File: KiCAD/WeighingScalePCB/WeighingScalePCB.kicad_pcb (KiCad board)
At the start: 2 copper layers, 94.6 x 73.3 mm, 64 parts, among them IC1 MAX6675ISA+T, IC2 APS11753KMDALX-9PL5, J1 Conn_01x14_MountingPin, J2 AudioJack4, J4 Battery Conn, J6 Conn_01x04_MountingPin, Q2 NX138AKR, Q3 NX138AKR, Q4 NX138AKR, Q5 NX138AKR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

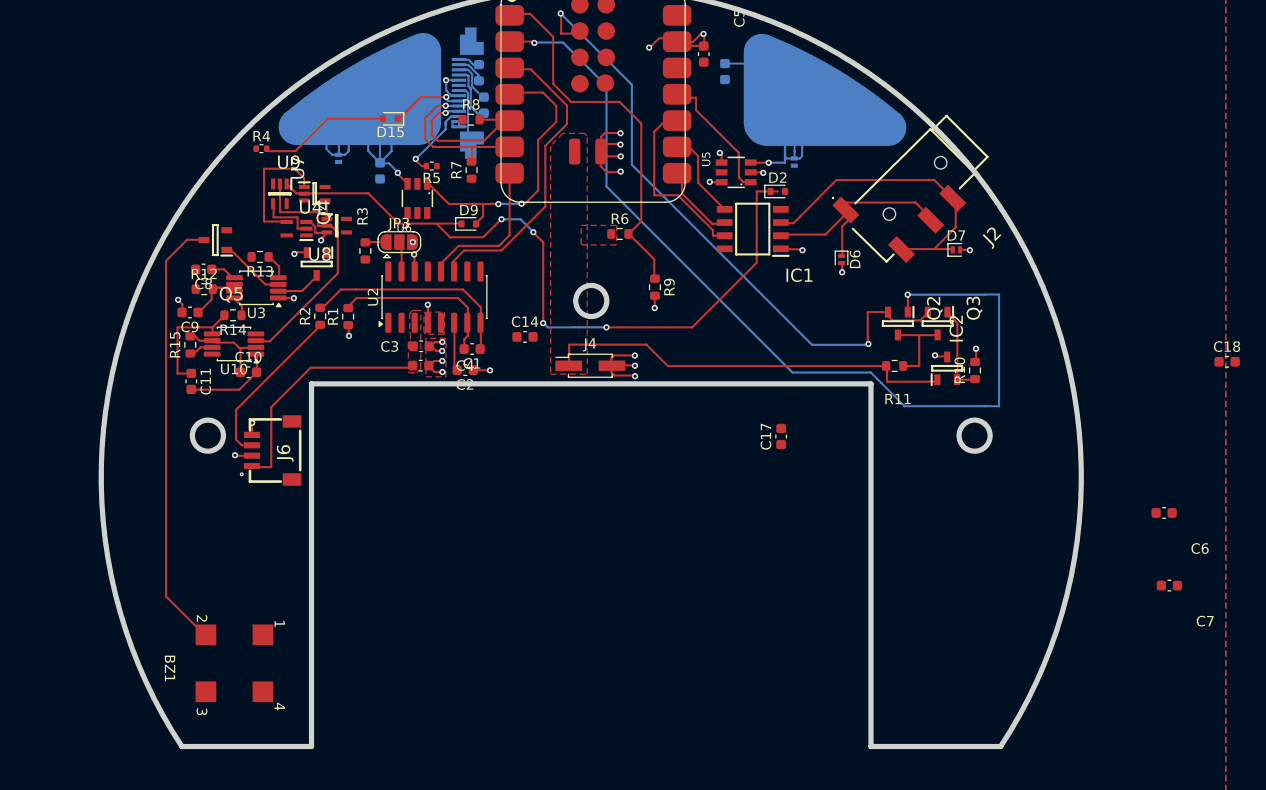
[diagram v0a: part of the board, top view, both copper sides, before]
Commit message: cleared all islands and unconnected GNDs, drc and erc pending, ferrite pending, linked 3d for thermocouple amp, touchpad ic and xiao
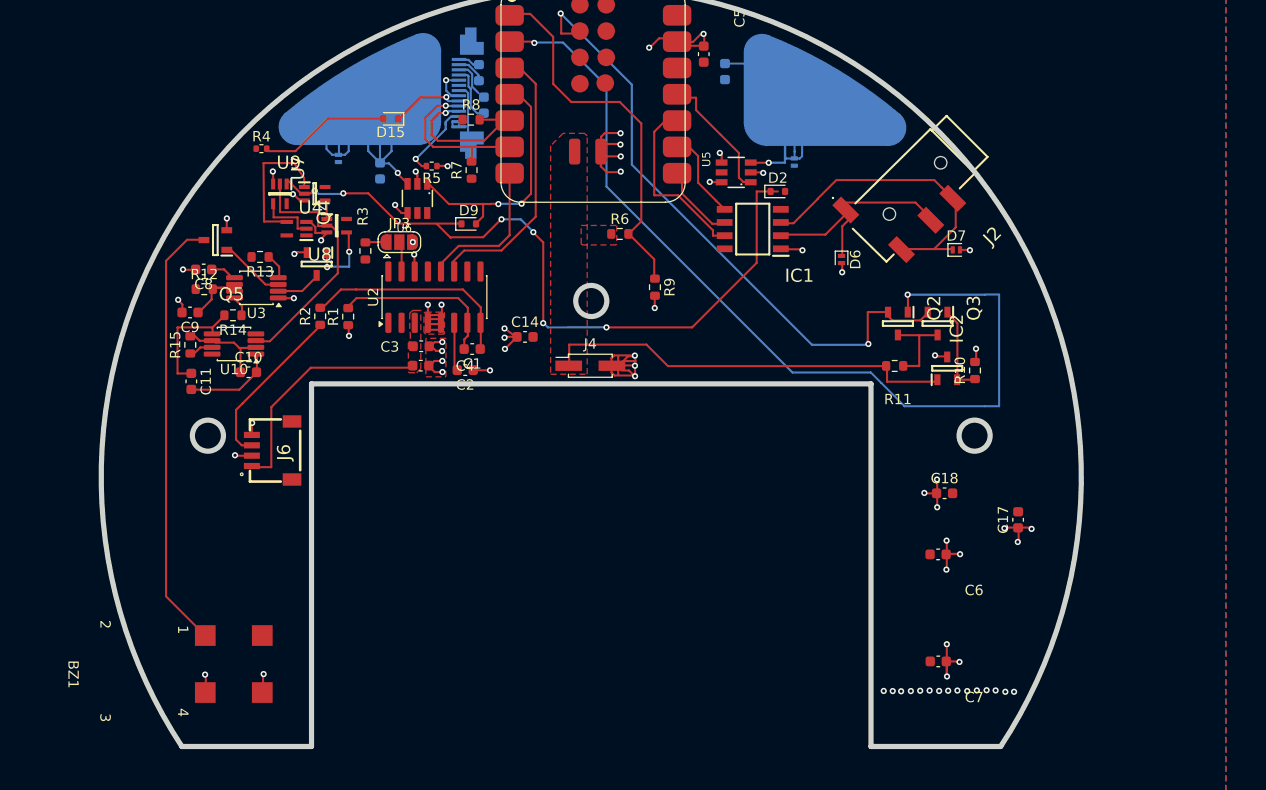
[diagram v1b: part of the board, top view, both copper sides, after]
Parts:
- moved C18 30.1 mm to (181.0, 85.6)
- moved C17 24.2 mm to (188.1, 88.2)
- moved C7 23.5 mm to (180.4, 101.9)
- moved C6 22.2 mm to (180.4, 91.5)
- moved BZ1 9.33 mm to (103.1, 102.6)
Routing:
- net GND: vias 33 -> 73
- net /timeORtare: vias 4 -> 6
- net /buzzer trigger: vias 0 -> 2

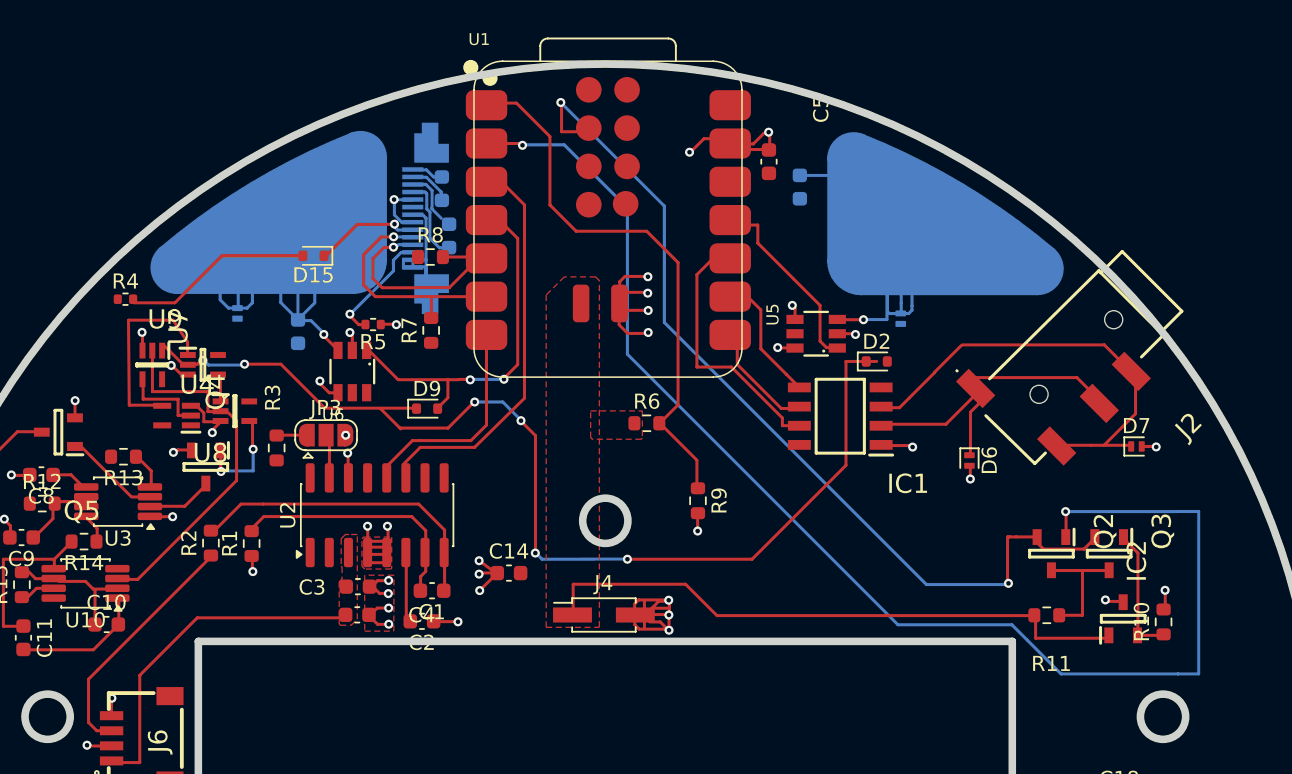
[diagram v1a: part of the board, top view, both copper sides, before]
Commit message: fb removed, decaps will be sufficient, add more decaps, add cap between vbat and vcc
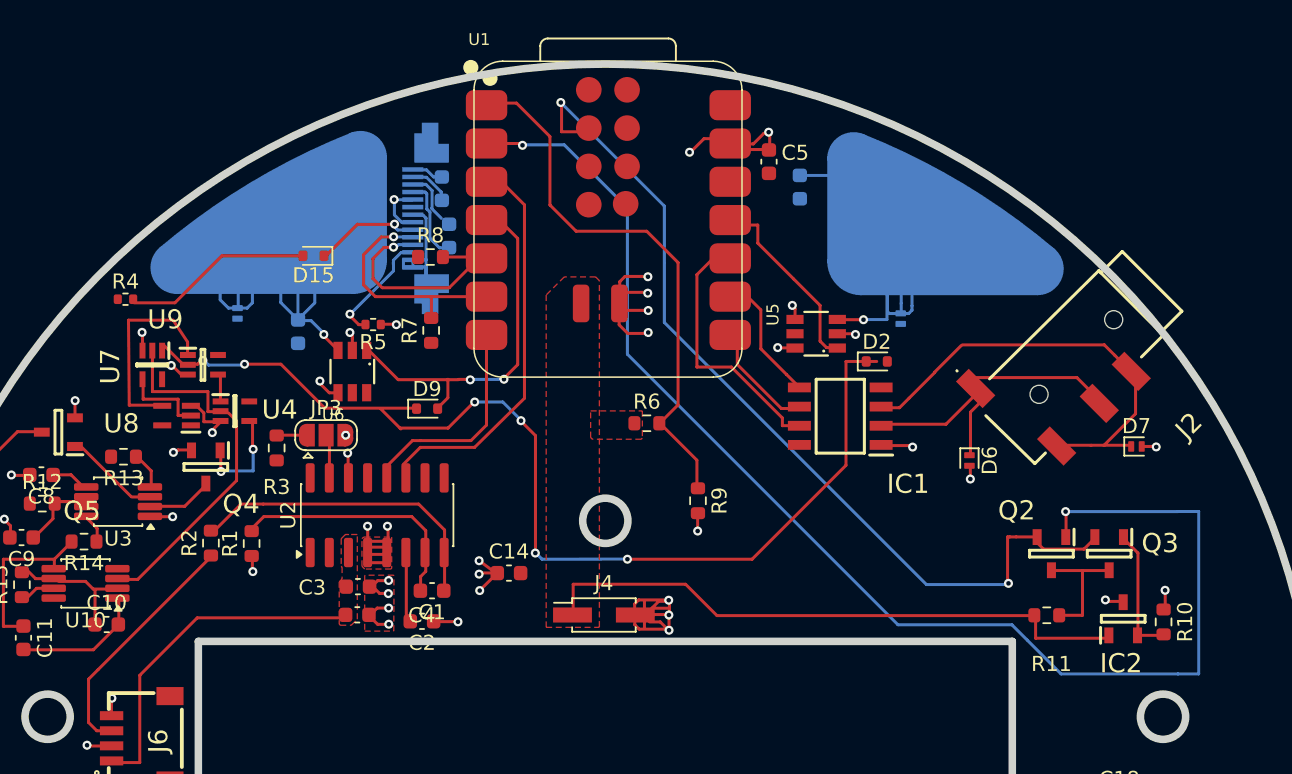
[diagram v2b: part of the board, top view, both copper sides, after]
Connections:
- C3 pad 2: /DVDD_ldcell -> VCC
- C4 pad 2: /DVDD_ldcell -> VCC
- J6 pad 1: /DVDD_ldcell -> VCC
- U2 pad 3: /DVDD_ldcell -> VCC
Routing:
- removed copper zone on F.Cu, net /DVDD_ldcell

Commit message: dxf to be updated, start design verification document next
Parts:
- moved C7 81.3 mm to (112.8, 56.7), turned to 90 degrees
- moved C6 78.7 mm to (103.5, 74.8), turned to 90 degrees
- moved C17 28.9 mm to (168.8, 66.6), turned to -90 degrees
- moved BZ1 20.9 mm to (96.8, 82.7)
- moved C18 14.1 mm to (189.9, 74.6), turned to 90 degrees
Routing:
- net GND: vias 73 -> 56

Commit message: all 3d added
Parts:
- moved C13 6.45 mm to (143.0, 48.6)
- moved C12 6.17 mm to (142.2, 44.5)
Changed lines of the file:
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@@
 		)
 		(group ""
-			(members "506a4490-bf3e-4c77-b169-08c29425c1eb" "5a118c7e-b5fb-4519-b66b-15accd4b80eb"
-				"6aae3fa3-525f-4afb-8aeb-590de53548be" "cf3bb025-e151-42ab-9bc5-0ee6cbb9af20"
-				"ebccb0a9-73e8-42e9-8617-28dd7e6247ca" "f4d772ca-2c29-4b5a-9d41-ad5a91ca73c4"
+			(members "068117ea-2ab3-4103-ba16-efab7a55a031" "22f2eacf-efce-438e-8243-23edad42cc39"
+				"6f3542f6-99f9-4a27-9b4c-fb9414b0d3b7" "7efa6883-bdff-4493-9e70-ba8cbb57e1ac"
+				"97dd7b8d-34f9-4bca-9663-b7264ed983fc" "d30c1f34-a56e-4f72-b701-78a4600fa9d7"
 			)
 		)
 		(group ""
-			(members "04d87761-6831-450b-a97a-65f3a226a256" "1311b18f-d4b6-42da-a0fc-41010944ea85"
-				"462201b0-c7be-4960-8844-6b6941b4ad2f" "6b9a12f5-451e-4911-b646-67a0598808ab"
-				"795389ad-acfc-4cde-b23d-8961354a9e65" "f49f4621-66a9-4145-a56a-5194f2d1576a"
+			(members "6514d6e0-6418-42fa-a38c-0725f87867d9" "6de8367c-d1df-4f82-a835-7e814d5bfa49"
+				"8147b97e-7544-4fa4-8697-c19391ba267f" "8179ba7d-6855-406b-b541-e840262d3c66"
+				"bbcafd73-0455-4559-b592-1946e72bc132" "db8d633d-4ceb-4d6e-b012-186990593e7a"
 			)
 		)
@@
 			)
 		)
+		(model "/home/chinmay/Projects/weighing_scale/Weighing-Scale-Coaster/KiCAD/WeighingScaleLibrary/LIB_SN74LVC1G04DCKR/SN74LVC1G04DCKR/3D/SN74LVC1G04DCKR.stp"
+			(offset
+				(xyz 0 0 0)
+			)
+			(scale
+				(xyz 1 1 1)
+			)
+			(rotate
+				(xyz 0 0 0)
+			)
+		)
 	)
 	(footprint "Footprints:SOT95P230X110-3N"
@@
 		)
 		(group ""
-			(members "04db45b0-54de-4ecb-b3c5-1046cf09671d" "441535aa-b818-4581-b5c3-c87ac78df74a"
-				"70dec69a-c15a-464d-b816-58cd609b9641" "a5ce6d7f-2c60-41db-8497-8040c0a304c2"
-				"e7423acd-4a56-4767-94b4-65c8eac0399b" "f55c3de0-39ea-4c4e-b807-f996b29d4372"
+			(members "56c2c2f2-41dc-4893-9ead-193c833977ec" "6f2889ef-8d5d-40c0-b0f0-e2c4b89dda04"
+				"70a92687-e41e-4280-9e15-a43491f83443" "79975846-58ba-4aca-bff2-32609abe09fe"
+				"9baa09ee-731b-4587-abcf-bb5f4ec44fb7" "ba98ae2b-0f4b-4403-9b40-e543a76478a0"
 			)
 		)
 		(group ""
-			(members "68e8b008-a0a5-43cd-b1f3-88e8a99a1445" "6ee33438-7f2b-4413-aa9f-a5a94c786fa7"
-				"7da6b385-5ffd-42e1-88ea-2362b0d28c88" "ac952bc0-21e2-4a34-98fa-b647f0e50b6c"
-				"b40dbc47-c785-419d-96d3-5da5963c95b4" "b410ba7d-2c2c-4c5e-af11-e89df746a8c0"
+			(members "2081a35a-ca3f-4472-a093-8e58f7bb1505" "445a45a7-f8a9-4c7b-834b-4eeea78861cd"
+				"66a930b3-a878-4489-8dda-2250efdb7383" "bb93f1d3-c7dd-4468-ba06-857c31f5a8c2"
+				"c3e7985c-49ec-4598-9838-d6b2f6419484" "f8dbbecf-a25a-4567-ba35-142d3adba851"
 			)
 		)
@@
 			)
 		)
+		(model "/home/chinmay/Projects/weighing_scale/Weighing-Scale-Coaster/KiCAD/WeighingScaleLibrary/LIB_74LVC1G79GW,125/74LVC1G79GW,125/3D/74LVC1G79GW,125.stp"
+			(offset
+				(xyz 1.5 0.9 -0.8)
+			)
+			(scale
+				(xyz 1 1 1)
+			)
+			(rotate
+				(xyz -90 -0 90)
+			)
+		)
 	)
 	(footprint "Diode_SMD:D_SOD-523"
@@
 			)
 		)
+		(model "/home/chinmay/Projects/weighing_scale/Weighing-Scale-Coaster/KiCAD/WeighingScaleLibrary/LIB_JST_SM04B-SRSS-TB_LF__SN_/SM04B-SRSS-TB_LF__SN_/3D/SM04B-SRSS-TB_LF__SN_.stp"
+			(offset
+				(xyz 3 4 -0.5)
+			)
+			(scale
+				(xyz 1 1 1)
+			)
+			(rotate
+				(xyz -90 -0 -0)
+			)
+		)
 	)
 	(footprint "Footprints:SOT95P240X115-3N_Hall effect"
@@
 			)
 		)
+		(model "/home/chinmay/Projects/weighing_scale/Weighing-Scale-Coaster/KiCAD/WeighingScaleLibrary/LIB_74LVC1G79GW,125/74LVC1G79GW,125/3D/74LVC1G79GW,125.stp"
+			(offset
+				(xyz 1.5 0.9 -0.8)
+			)
+			(scale
+				(xyz 1 1 1)
+			)
+			(rotate
+				(xyz -90 -0 90)
+			)
+		)
 	)
 	(footprint "Resistor_SMD:R_0603_1608Metric"
@@
 			)
 		)
+		(model "/home/chinmay/Projects/weighing_scale/Weighing-Scale-Coaster/KiCAD/WeighingScaleLibrary/LIB_SFV14R-3STBE1HLF/SFV14R-3STBE1HLF/3D/SFV14R-3STBE1HLF.stp"
+			(offset
+				(xyz 5.45 -4.3 2)
+			)
+			(scale
+				(xyz 1 1 1)
+			)
+			(rotate
+				(xyz 90 -0 180)
+			)
+		)
 	)
 	(footprint "Capacitor_SMD:C_0603_1608Metric"
 		(layer "B.Cu")
-		(at 136.04 45.035 90)
+		(at 142.19 44.48 90)
 		(descr "Capacitor SMD 0603 (1608 Metric), square (rectangular) end terminal, IPC-7351 nominal, (Body size source: IPC-SM-782 page 76, https://www.pcb-3d.com/wordpress/wp-content/uploads/ipc-sm-782a_amendment_1_and_2.pdf), generated with kicad-footprint-generator")
 		(tags "capacitor")
@@
 	(footprint "Capacitor_SMD:C_0603_1608Metric"
 		(layer "B.Cu")
-		(at 136.52 48.17 -90)
+		(at 142.96 48.58 -90)
 		(descr "Capacitor SMD 0603 (1608 Metric), square (rectangular) end terminal, IPC-7351 nominal, (Body size source: IPC-SM-782 page 76, https://www.pcb-3d.com/wordpress/wp-content/uploads/ipc-sm-782a_amendment_1_and_2.pdf), generated with kicad-footprint-generator")
 		(tags "capacitor")
@@
 	)
 	(gr_line
+		(start 141.44 43.77)
+		(end 142.21 43.77)
+		(stroke
+			(width 0.2)
+			(type default)
+		)
+		(layer "B.Cu")
+		(net 39)
+	)
+	(gr_line
 		(start 164.02 53.72)
 		(end 165.57 53.72)
@@
 	)
 	(gr_line
+		(start 136.62 48.96)
+		(end 141.52 48.96)
+		(stroke
+			(width 0.2)
+			(type default)
+		)
+		(layer "B.Cu")
+		(net 61)
+	)
+	(gr_line
 		(start 167.23 53.1)
 		(end 167.23 52.8)
@@
 	)
 	(gr_line
+		(start 140.95 44.26)
+		(end 141.44 43.77)
+		(stroke
+			(width 0.2)
+			(type default)
+		)
+		(layer "B.Cu")
+		(net 39)
+	)
+	(gr_line
+		(start 135.64 46.6)
+		(end 135.64 47.69)
+		(stroke
+			(width 0.2)
+			(type default)
+		)
+		(layer "B.Cu")
+		(net 60)
+	)
+	(gr_line
 		(start 134.99 50.23)
 		(end 134.99 51.13)
@@
 	)
 	(gr_line
+		(start 135.39 46.35)
+		(end 135.64 46.6)
+		(stroke
+			(width 0.2)
+			(type default)
+		)
+		(layer "B.Cu")
+		(net 60)
+	)
+	(gr_line
 		(start 127.61 52.61)
 		(end 127.61 51.65)
@@
 	)
 	(gr_line
+		(start 141.52 48.96)
+		(end 142.03 49.47)
+		(stroke
+			(width 0.2)
+			(type default)
+		)
+		(layer "B.Cu")
+		(net 61)
+	)
+	(gr_line
 		(start 134.16 44.75)
 		(end 134.98 44.75)
@@
 	)
 	(gr_line
+		(start 136 45.26)
+		(end 142.21 45.26)
+		(stroke
+			(width 0.2)
+			(type default)
+		)
+		(layer "B.Cu")
+		(net 38)
+	)
+	(gr_line
 		(start 134.99 51.13)
 		(end 134.99 49.75)
@@
 	)
 	(gr_line
+		(start 142.03 49.47)
+		(end 142.96 49.47)
+		(stroke
+			(width 0.2)
+			(type default)
+		)
+		(layer "B.Cu")
+	)
+	(gr_line
 		(start 134.15 49.27)
 		(end 133.34 49.27)
@@
 		)
 		(layer "B.Cu")
+		(net 61)
 	)
 	(gr_line
@@
 	)
 	(gr_line
+		(start 135.64 47.69)
+		(end 142.94 47.69)
+		(stroke
+			(width 0.2)
+			(type default)
+		)
+		(layer "B.Cu")
+	)
+	(gr_line
 		(start 123.12 52.96)
 		(end 123.47 52.61)
@@
 	)
 	(gr_line
-		(start 134.1 44.28)
-		(end 135.02 44.28)
+		(start 136.08 44.26)
+		(end 140.95 44.26)
 		(stroke
 			(width 0.2)
@@
 		)
 		(layer "B.Cu")
-		(net 38)
+		(net 39)
 	)
 	(gr_line
-		(start 135.35 46.35)
-		(end 136.01 47.01)
+		(start 134.1 44.28)
+		(end 135.02 44.28)
 		(stroke
 			(width 0.2)
@@
 		)
 		(layer "B.Cu")
+		(net 38)
 	)
 	(gr_line
@@
 	)
 	(gr_line
-		(start 136 45.26)
-		(end 136 45.71)
-		(stroke
-			(width 0.2)
-			(type default)
-		)
-		(layer "B.Cu")
-		(net 38)
-	)
-	(gr_line
